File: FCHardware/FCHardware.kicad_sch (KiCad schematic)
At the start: 46 parts, among them J1 JST-8pin, J3 USB_C_Receptacle_USB2.0_16P, SW4 SW_Push, U1 STM32F405RGTx, U3 ICM-42688-P, U4 TPSM63603, U5 ESC_Xrotor_65A_4in1, U9 USBLC6-2SC6

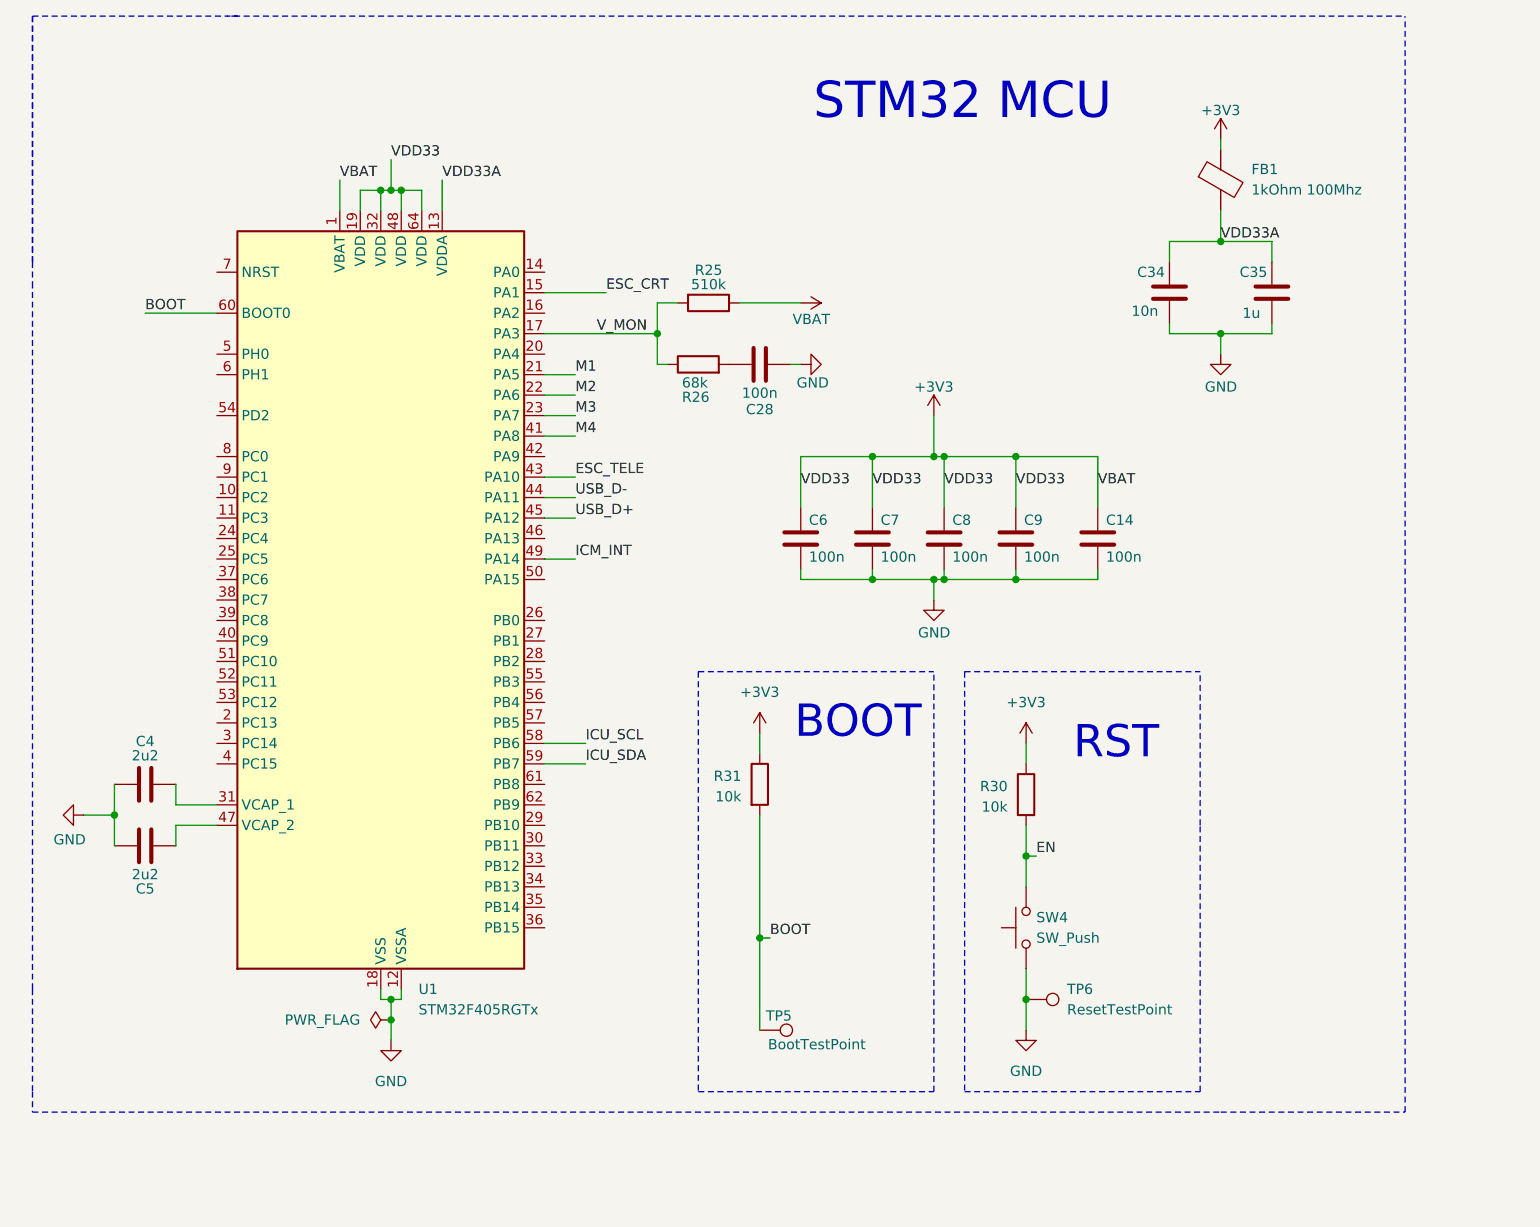
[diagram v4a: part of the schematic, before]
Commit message: Fixed RST and BOOT sequences, wired STM32
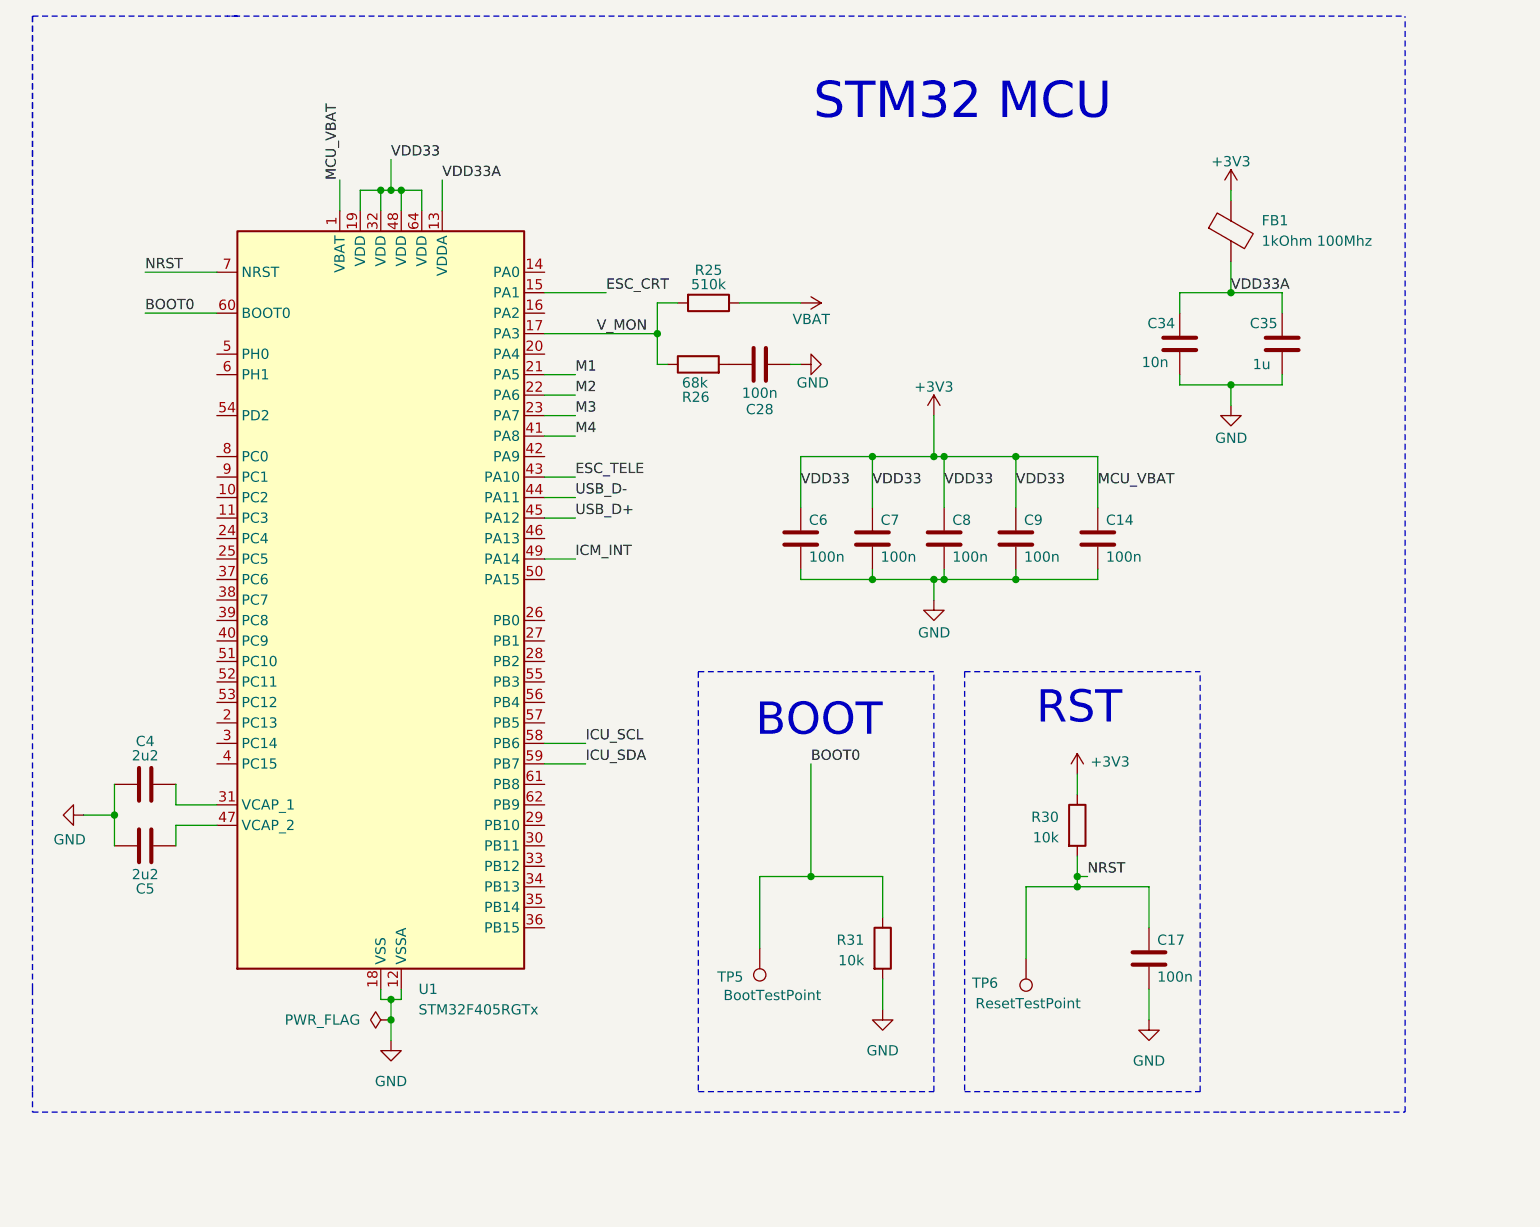
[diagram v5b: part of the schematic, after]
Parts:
- removed SW4: SW_Push, Button_Switch_THT:SW_PUSH_6mm, symbol Switch:SW_Push
- added C17: 100n, symbol Device:C
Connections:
- net EN is gone; now on net NRST: R30.2
- net +3V3: no longer C10.2, C11.2, C16.2, D1.2 (A), J1.7 (Pin_7), R25.1, R31.1, U4.2 (EN/SYNC), U4.3 (VIN), U4.4 (VIN), U5.3 (VBAT+)
- net GND: now also R31.2, C17.2; no longer TP6.1
- net NRST: now reaches U1.7 (NRST)
- net NRST: now also TP6.1, C17.1
- net BOOT renamed BOOT0
- net BOOT0: now also R31.1; no longer R31.2
- new net VBAT: C10.2, C11.2, C16.2, D1.2 (A), J1.7 (Pin_7), R25.1, U4.2 (EN/SYNC), U4.3 (VIN), U4.4 (VIN), U5.3 (VBAT+)
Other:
- moved on the sheet: C34, C35, FB1, R30, TP5, TP6

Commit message: Added reciever, separated 3v3 and 5v rails
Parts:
- added C18: 22u, Capacitor_SMD:C_1206_3216Metric_Pad1.33x1.80mm_HandSolder, symbol Device:C
- added C19, C20: 1u, symbol Device:C
- added J2: JST-4pin, symbol Connector:Conn_01x04_Pin
- added U2: AP2112K-3.3, Package_TO_SOT_SMD:SOT-23-5, symbol Regulator_Linear:AP2112K-3.3
- R11: value 27.4k -> 13k
- R12: value 23.2k -> 40.2k
- TP3: value 3V3TestPoint -> 5VTestPoint
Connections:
- net ICU_INT is gone; now on net IMU_INT: U3.4 (INT1/INT)
- net +3V3: now also C20.2, U2.5 (VOUT); no longer C15.1, R12.2, TP3.1, U4.10 (VOUT), U4.12 (VOUT), U4.13 (VOUT), U4.14 (VOUT), U4.15 (VOUT), U4.22 (VLDOIN), U4.7 (VOUT), U4.8 (VOUT), U4.9 (VOUT)
- net GND: now also C18.2, C19.2, C20.1, J2.1 (Pin_1), U2.2 (GND); no longer U3.1 (AP_SDO/AP_AD0)
- net IMU_CS: now reaches U3.12 (AP_CS)
- net IMU_CS: now also U1.27 (PB1)
- net IMU_INT: now reaches U1.26 (PB0)
- net RC_RX: now reaches U1.29 (PB10)
- net RC_RX: now also J2.4 (Pin_4)
- net RC_TX: now reaches U1.30 (PB11)
- net RC_TX: now also J2.3 (Pin_3)
- net IMU_SDI: now reaches U1.56 (PB4)
- net IMU_SDI: now also U3.14 (AP_SDA/AP_SDIO/AP_SDI)
- net IMU_SDO: now reaches U1.57 (PB5)
- net IMU_SDO: now also U3.1 (AP_SDO/AP_AD0)
- net ICM_INT: no longer names the net of U1.49 (PA14)
- net ICU_SCL renamed IMU_SCLK
- net ICU_SDA: no longer names the net of U1.59 (PB7)
- net ICU_SDA: no longer U3.14 (AP_SDA/AP_SDIO/AP_SDI)
- new net +5V: C15.1, C18.1, C19.1, J2.2 (Pin_2), R12.2, TP3.1, U2.1 (VIN), U2.3 (EN), U4.10 (VOUT), U4.12 (VOUT), U4.13 (VOUT), U4.14 (VOUT), U4.15 (VOUT), U4.22 (VLDOIN), U4.7 (VOUT), U4.8 (VOUT), U4.9 (VOUT)
- no-connect marks 15 -> 50
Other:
- note added: "5V to 3V3 LDO"
- note added: "BATT to 5V Buck"
- note added: "Reciever JST Connector"
- note removed: "BATT to 3V3 Converter"
- moved on the sheet: C15, H1, H2, H3, H4, J3, R28, R29, TP3, U9

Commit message: Fixed ERC errors
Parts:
- U4: footprint FCFootprints:CONV_TPSM63603EXTRDHR -> RF_Module:ESP32-C3-WROOM-02
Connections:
- no-connect marks 50 -> 55
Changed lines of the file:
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@@
 	)
 	(junction
+		(at 87.63 46.99)
+		(diameter 0)
+		(color 0 0 0 0)
+	)
+	(junction
 		(at 191.77 231.14)
 		(diameter 0)
@@
 	)
 	(no_connect
+		(at 93.98 250.19)
+	)
+	(no_connect
 		(at 100.33 78.74)
 	)
@@
 	)
 	(no_connect
+		(at 43.18 237.49)
+	)
+	(no_connect
 		(at 379.73 66.04)
 	)
@@
 	)
 	(no_connect
+		(at 93.98 245.11)
+	)
+	(no_connect
 		(at 59.69 83.82)
 	)
@@
 	)
 	(no_connect
+		(at 93.98 247.65)
+	)
+	(no_connect
 		(at 100.33 106.68)
 	)
@@
 	)
 	(no_connect
+		(at 93.98 242.57)
+	)
+	(no_connect
 		(at 100.33 93.98)
 	)
@@
 	(wire
 		(pts
-			(xy 87.63 44.45) (xy 87.63 48.26)
+			(xy 87.63 44.45) (xy 87.63 46.99)
 		)
 		(stroke
@@
 		)
 	)
+	(wire
+		(pts
+			(xy 87.63 46.99) (xy 87.63 48.26)
+		)
+		(stroke
+			(width 0)
+			(type default)
+		)
+	)
 	(polyline
 		(pts
@@
 	)
 	(symbol
+		(lib_id "power:PWR_FLAG")
+		(at 87.63 46.99 270)
+		(unit 1)
+		(exclude_from_sim no)
+		(in_bom yes)
+		(on_board yes)
+		(dnp no)
+		(fields_autoplaced yes)
+		(property "Reference" "#FLG06"
+			(at 89.535 46.99 0)
+			(effects
+				(font
+					(size 1.27 1.27)
+				)
+				(hide yes)
+			)
+		)
+		(property "Value" "PWR_FLAG"
+			(at 91.44 46.9899 90)
+			(effects
+				(font
+					(size 1.27 1.27)
+				)
+				(justify left)
+			)
+		)
+		(property "Footprint" ""
+			(at 87.63 46.99 0)
+			(effects
+				(font
+					(size 1.27 1.27)
+				)
+				(hide yes)
+			)
+		)
+		(property "Datasheet" "~"
+			(at 87.63 46.99 0)
+			(effects
+				(font
+					(size 1.27 1.27)
+				)
+				(hide yes)
+			)
+		)
+		(property "Description" "Special symbol for telling ERC where power comes from"
+			(at 87.63 46.99 0)
+			(effects
+				(font
+					(size 1.27 1.27)
+				)
+				(hide yes)
+			)
+		)
+		(pin "1"
+		)
+		(instances
+			(project ""
+				(path "/2c9190cb-62a9-4a80-bcd5-31c54a1af4fd"
+					(reference "#FLG06")
+					(unit 1)
+				)
+			)
+		)
+	)
+	(symbol
 		(lib_id "Device:C")
 		(at 132.08 88.9 0)
@@
 			)
 		)
-		(property "Footprint" "FCFootprints:CONV_TPSM63603EXTRDHR"
+		(property "Footprint" "RF_Module:ESP32-C3-WROOM-02"
 			(at 344.17 207.645 0)
 			(effects

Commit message: Updated BoM
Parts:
- renumbered C4 to C1, C9 to C10, C14 to C11, C17 to C12, C34 to C13, C35 to C14, C19 to C15, C20 to C16, C10 to C17, C11 to C18, C16 to C19, C5 to C2, C12 to C20, C15 to C21, C13 to C22, C18 to C23, C1 to C3, C2 to C4, C3 to C5, C28 to C6, C6 to C7, C7 to C8, C8 to C9, J3 to J1, J1 to J3, R26 to R1, R25 to R2, R31 to R3, R30 to R4, R28 to R5, R29 to R6, R11 to R7, R12 to R8, R13 to R9, TP5 to TP1, TP6 to TP2, TP2 to TP3, TP3 to TP4, U3 to U1, U1 to U2, U9 to U3, U2 to U4, U4 to U5, U5 to U6
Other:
- note added: "Receiver JST Connector"
- note removed: "Reciever JST Connector"
